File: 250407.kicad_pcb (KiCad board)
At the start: 2 copper layers, 390 x 180.2 mm, 227 parts, among them CN1 KEYBOARD_20PIN_MALE, CN10 LED_CONNECTOR, CN2 USER_PORT_CON, CN3 CASSETTE_PORT_CON, CN4 SERIAL_BUS_CON, CN5 AV_CONN, CN6 EXPANSION_PORT, CN7 POWER_CON, CN8 CONTROL_PORT, CN9 CONTROL_PORT, M1 MODULATOR_LONGBOARD, Q1 2SC1815, Q2 2SC1815, Q3 TP29B/2SD880, Q7 2SC1815, Q8 2SC1815, SW1 POWER_SWITCH, U1 CIA_U1, U10 4164-2, U11 4164-2, U12 4164-2, U13 74LS257, U14 74LS258, U15 74LS139, U16 4066_U28, U17 PLA_U17, U18 6581, U19 VIC, U2 CIA_U2, U20 556, U21 4164-2, U22 4164-2, U23 4164-2, U24 4164-2, U25 74LS257, U26 74LS373, U27 7408_U27, U28 4066_U28, U29 74LS74, U3 2364A, U30 74LS193, U31 74LS629N, U32 MC4044, U4 2364A, U5 2332A, U6 2114, U7 6510_MPU, U8 7406N, U9 4164-2, Y1 Crystal

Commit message: rename schematics and pcb libraries add C64-discrete-library for the missing symbols fix symbol references in sch and pcb
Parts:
- C1, C10, C100, C101, C103, C105, C11, C16, C18, C2, C200, C204, C205, C22, C25, C26, C27, C28, C29, C3, C30, C31, C32, C33, C37, C39, C4, C40, C41, C42, C43, C44, C45, C46, C47, C48, C49, C5, C50, C51, C52, C53, C54, C56, C59, C6, C60, C66, C67, C68, C7, C74, C82, C84, C85, C89, C9, C92, C93, C95, C96, C97, C98, C99: footprint KU-14194HB-RevB-KiCad:CAP_P5.08mm -> C64-pcb-library:CAP_P5.08mm
- C102, C107, C108, C12, C13, C14, C15, C17, C24, C34, C57, C62, C65, C8, C94: footprint KU-14194HB-RevB-KiCad:CAP_ELYT_RADIAL_P5.08mm_SMALL_RING -> C64-pcb-library:CAP_ELYT_RADIAL_P5.08mm_SMALL_RING
- C19, C88, C90: footprint KU-14194HB-RevB-KiCad:LARGE_ELECTROLYTIC_AXIAL_TH -> C64-pcb-library:LARGE_ELECTROLYTIC_AXIAL_TH
- C20, C21: footprint KU-14194HB-RevB-KiCad:CAP_POLY_100V_TH_P5.08_and_P12.07mm -> C64-pcb-library:CAP_POLY_100V_TH_P5.08_and_P12.07mm
- C203: footprint KU-14194HB-RevB-KiCad:CAPACITOR_RADIAL_P13.97_L9.9_D3.6 -> C64-pcb-library:CAPACITOR_RADIAL_P13.97_L9.9_D3.6
- C23, C38: footprint KU-14194HB-RevB-KiCad:CAP_AXIAL_P12.7mm -> C64-pcb-library:CAP_AXIAL_P12.7mm
- C36, C70, C83, C86, L2, R1, R100, R16, R17, R19, R2, R26, R28, R29, R3, R30, R31, R33, R34, R35, R36, R37, R38, R39, R4, R41, R42, R43, R44, R45, R5, R50, R51, R52, R53, R6, R7: footprint KU-14194HB-RevB-KiCad:RESISTOR -> C64-pcb-library:RESISTOR
- C91: footprint KU-14194HB-RevB-KiCad:CAP_ELYT_RADIAL_P5.08mm -> C64-pcb-library:CAP_ELYT_RADIAL_P5.08mm
- CN1: footprint KU-14194HB-RevB-KiCad:KEYBOARD_CON -> C64-pcb-library:KEYBOARD_CON
- CN10: footprint KU-14194HB-RevB-KiCad:LED_CON -> C64-pcb-library:LED_CON
- CN2: footprint KU-14194HB-RevB-KiCad:EDGE_CON_24P -> C64-pcb-library:EDGE_CON_24P
- CN3: footprint KU-14194HB-RevB-KiCad:EDGE_CON_12P_TAPE -> C64-pcb-library:EDGE_CON_12P_TAPE
- CN4: footprint KU-14194HB-RevB-KiCad:SERIAL_CON_DIN6 -> C64-pcb-library:SERIAL_CON_DIN6
- CN5: footprint KU-14194HB-RevB-KiCad:AV_CON_DIN8 -> C64-pcb-library:AV_CON_DIN8
- CN6: footprint KU-14194HB-RevB-KiCad:EXPANSION_PORT -> C64-pcb-library:EXPANSION_PORT
- CN7: footprint KU-14194HB-RevB-KiCad:POWER_CON_D7_250407 -> C64-pcb-library:POWER_CON_D7_250407
- CN8, CN9: footprint KU-14194HB-RevB-KiCad:JOYPORT_DB9 -> C64-pcb-library:JOYPORT_DB9
- CR1, CR2: footprint KU-14194HB-RevB-KiCad:ZENER_12.7mm -> C64-pcb-library:ZENER_12.7mm
- CR4: footprint KU-14194HB-RevB-KiCad:BRIDGE_RECTIFIER -> C64-pcb-library:BRIDGE_RECTIFIER
- CR5, CR6: footprint KU-14194HB-RevB-KiCad:RECTIFIER_TH_P12.7mm -> C64-pcb-library:RECTIFIER_TH_P12.7mm
- E1, E2: footprint KU-14194HB-RevB-KiCad:JUMPER_WIRE -> C64-pcb-library:JUMPER_WIRE
- F1: footprint KU-14194HB-RevB-KiCad:FUSE -> C64-pcb-library:FUSE
- FB1, FB10, FB11, FB12, FB13, FB14, FB15, FB16, FB17, FB18, FB19, FB2, FB20, FB21, FB22, FB23, FB3, FB4, FB5, FB7, FB8, FB9: footprint KU-14194HB-RevB-KiCad:FERRITE_BEAD_TH_P12.7mm -> C64-pcb-library:FERRITE_BEAD_TH_P12.7mm
- L4: footprint KU-14194HB-RevB-KiCad:CHOKE -> C64-pcb-library:CHOKE
- L5: footprint KU-14194HB-RevB-KiCad:INDUCTOR_P15.24mm -> C64-pcb-library:INDUCTOR_P15.24mm
- M1: footprint KU-14194HB-RevB-KiCad:MODULATOR_PORT_LONGBOARD -> C64-pcb-library:MODULATOR_PORT_LONGBOARD
- Q1, Q2, Q7, Q8: footprint KU-14194HB-RevB-KiCad:Q_NPN_ECB -> C64-pcb-library:Q_NPN_ECB
- Q3: footprint KU-14194HB-RevB-KiCad:TO-220-3_Horizontal_TabDown_250407 -> C64-pcb-library:TO-220-3_Horizontal_TabDown_250407
- R27: footprint KU-14194HB-RevB-KiCad:POTMETER -> C64-pcb-library:POTMETER
- RP1, RP2, RP3: footprint KU-14194HB-RevB-KiCad:RP_ARRAY_7WAY -> C64-pcb-library:RP_ARRAY_7WAY
- RP4: footprint KU-14194HB-RevB-KiCad:RP_ARRAY_9WAY -> C64-pcb-library:RP_ARRAY_9WAY
- SW1: footprint KU-14194HB-RevB-KiCad:POWER_SWITCH -> C64-pcb-library:POWER_SWITCH
- U1, U19, U2, U7: footprint KU-14194HB-RevB-KiCad:DIP40 -> C64-pcb-library:DIP40
- U10, U11, U12, U13, U14, U15, U21, U22, U23, U24, U25, U30, U31, U9: footprint KU-14194HB-RevB-KiCad:DIP16 -> C64-pcb-library:DIP16
- U16, U20, U27, U28, U29, U32, U8: footprint KU-14194HB-RevB-KiCad:DIP14 -> C64-pcb-library:DIP14
- U17, U18: footprint KU-14194HB-RevB-KiCad:DIP28 -> C64-pcb-library:DIP28
- U26: footprint KU-14194HB-RevB-KiCad:DIP20 -> C64-pcb-library:DIP20
- U3, U4, U5: footprint KU-14194HB-RevB-KiCad:DIP24 -> C64-pcb-library:DIP24
- U6: footprint KU-14194HB-RevB-KiCad:DIP18 -> C64-pcb-library:DIP18
- VR1, VR2: footprint KU-14194HB-RevB-KiCad:VREG_TO-220-3_Horizontal_TabDown -> C64-pcb-library:VREG_TO-220-3_Horizontal_TabDown
- Y1: footprint KU-14194HB-RevB-KiCad:CRYSTAL -> C64-pcb-library:CRYSTAL
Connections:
- C1 pad 1: /5V_FB3 -> Net-(C1-Pad1)
- C66 pad 1: CAN+5V -> Net-(C66-Pad1)
- C67 pad 1: /+Vc -> Net-(C67-Pad1)
- C82 pad 1: /+Vc -> Net-(C82-Pad1)
- CN7 pad 2: Earth -> Net-(CN7-Pad2)
- E1 pad 2: /jumper_select -> Net-(E1-Pad2)
- R27 pad 3: Net-(C108-Pad1) -> Net-(R27-Pad3)
- SW1 pad pe: (no net) -> Earth
- U27 pad 14: +5V -> Net-(U27-Pad14)
- U29 pad 1: Earth -> Net-(U29-Pad1)
- U29 pad 2: Earth -> Net-(U29-Pad2)
- U31 pad 1: Net-(C108-Pad1) -> Net-(R27-Pad3)

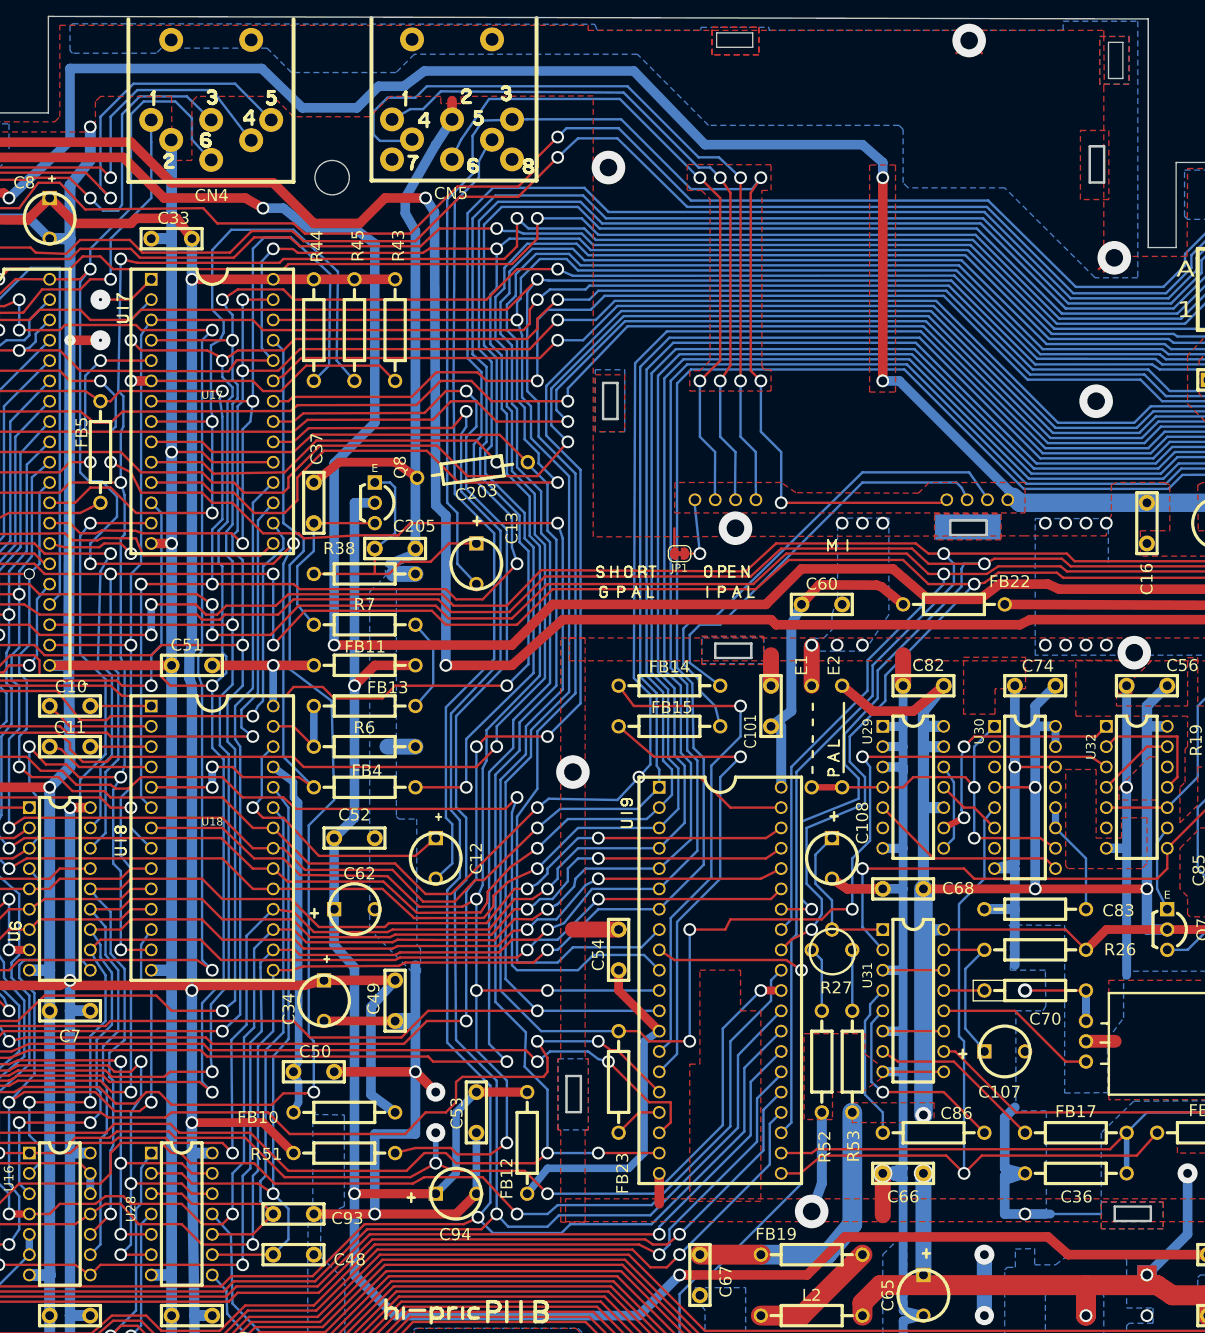
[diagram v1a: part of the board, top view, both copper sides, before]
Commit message: change Earth net to GND fix PCB DRC fix slanted PCB edge
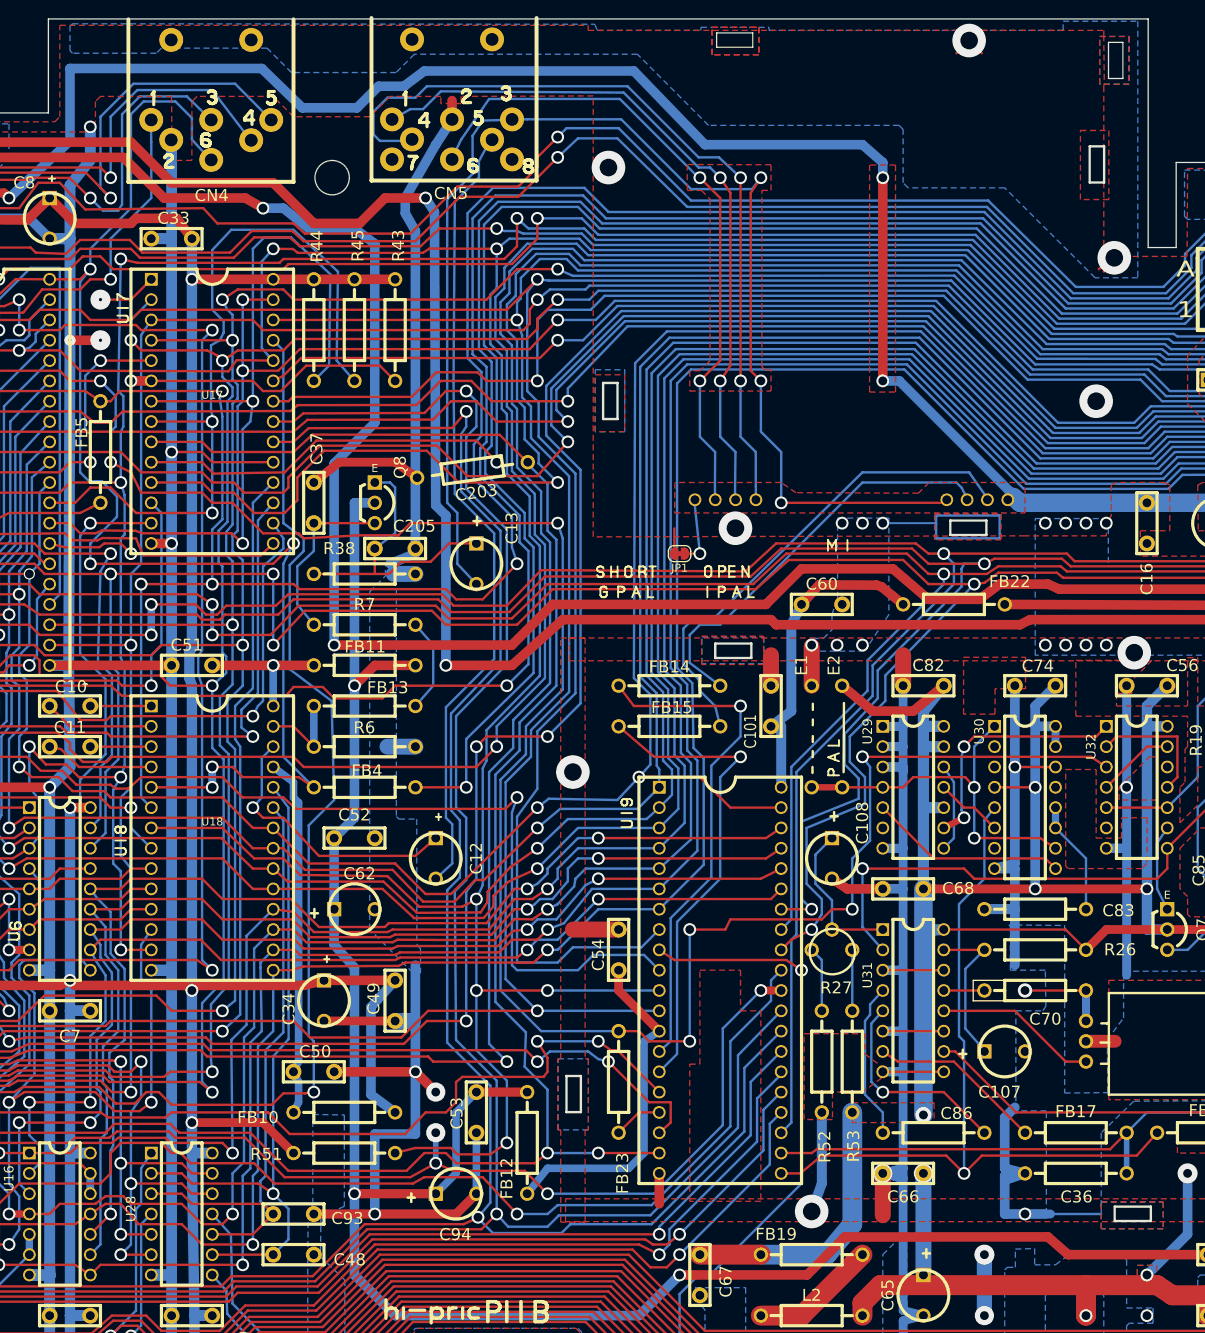
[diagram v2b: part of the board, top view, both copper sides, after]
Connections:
- C1 pad 1: Net-(C1-Pad1) -> /5V_FB3
- C1 pad 2: Earth -> GND
- C100 pad 1: Earth -> GND
- C101 pad 2: Earth -> GND
- C102 pad 2: Earth -> GND
- C103 pad 2: Earth -> GND
- C105 pad 1: Earth -> GND
- C107 pad 2: Earth -> GND
- C108 pad 2: Earth -> GND
- C14 pad 2: Earth -> GND
- C15 pad 2: Earth -> GND
- C16 pad 2: Earth -> GND
- C17 pad 2: Earth -> GND
- C19 pad 2: Earth -> GND
- C2 pad 2: Earth -> GND
- C200 pad 2: Earth -> GND
- C203 pad 1: Earth -> GND
- C204 pad 1: Earth -> GND
- C205 pad 2: Earth -> GND
- C22 pad 2: Earth -> GND
- C23 pad 2: Earth -> GND
- C24 pad 2: Earth -> GND
- C25 pad 2: Earth -> GND
- C26 pad 2: Earth -> GND
- C27 pad 2: Earth -> GND
- C28 pad 2: Earth -> GND
- C29 pad 1: Earth -> GND
- C3 pad 1: Earth -> GND
- C30 pad 2: Earth -> GND
- C31 pad 1: Earth -> GND
- C32 pad 1: Earth -> GND
- C33 pad 2: Earth -> GND
- C34 pad 2: Earth -> GND
- C36 pad 2: Earth -> GND
- C37 pad 2: Earth -> GND
- C39 pad 1: Earth -> GND
- C4 pad 1: Earth -> GND
- C40 pad 2: Earth -> GND
- C41 pad 2: Earth -> GND
- C42 pad 2: Earth -> GND
- C43 pad 2: Earth -> GND
- C44 pad 1: Earth -> GND
- C45 pad 2: Earth -> GND
- C46 pad 2: Earth -> GND
- C47 pad 2: Earth -> GND
- C48 pad 2: Earth -> GND
- C49 pad 2: Earth -> GND
- C5 pad 1: Earth -> GND
- C50 pad 2: Earth -> GND
- C51 pad 2: Earth -> GND
- C52 pad 2: Earth -> GND
- C53 pad 2: Earth -> GND
- C54 pad 2: Earth -> GND
- C56 pad 2: Earth -> GND
- C57 pad 2: Earth -> GND
- C59 pad 2: Earth -> GND
- C6 pad 1: Earth -> GND
- C60 pad 2: Earth -> GND
- C62 pad 2: Earth -> GND
- C65 pad 2: Earth -> GND
- C66 pad 1: Net-(C66-Pad1) -> CAN+5V
- C66 pad 2: Earth -> GND
- C67 pad 1: Net-(C67-Pad1) -> /+Vc
- C67 pad 2: Earth -> GND
- C68 pad 2: Earth -> GND
- C7 pad 2: Earth -> GND
- C74 pad 2: Earth -> GND
- C8 pad 2: Earth -> GND
- C82 pad 1: Net-(C82-Pad1) -> /+Vc
- C82 pad 2: Earth -> GND
- C83 pad 2: Earth -> GND
- C84 pad 2: Earth -> GND
- C88 pad 2: Earth -> GND
- C89 pad 2: Earth -> GND
- C9 pad 2: Earth -> GND
- C91 pad 2: Earth -> GND
- C92 pad 2: Earth -> GND
- C93 pad 2: Earth -> GND
- C94 pad 2: Earth -> GND
- C95 pad 2: Earth -> GND
- C96 pad 1: Earth -> GND
- C97 pad 1: Earth -> GND
- C98 pad 2: Earth -> GND
- C99 pad 1: Earth -> GND
- CN1 pad 1: Earth -> GND
- CN2 pad 1: Earth -> GND
- CN2 pad 12: Earth -> GND
- CN2 pad A: Earth -> GND
- CN2 pad N: Earth -> GND
- CN3 pad A,1: Earth -> GND
- CN4 pad 2: Earth -> GND
- CN5 pad 2: Earth -> GND
- CN6 pad 1: Earth -> GND
- CN6 pad 22: Earth -> GND
- CN6 pad A: Earth -> GND
- CN6 pad Z: Earth -> GND
- CN7 pad 1: Earth -> GND
- CN7 pad 3: Earth -> GND
- CN8 pad 8: Earth -> GND
- CN9 pad 8: Earth -> GND
- CR1 pad 2: Earth -> GND
- CR2 pad 2: Earth -> GND
- CR4 pad 3: Earth -> GND
- E1 pad 1: Earth -> GND
- E1 pad 2: Net-(E1-Pad2) -> /jumper_select
- FB20 pad 1: Earth -> GND
- JP1 pad 2: Earth -> GND
- Q2 pad 1: Earth -> GND
- R27 pad 3: Net-(R27-Pad3) -> Net-(C108-Pad1)
- R3 pad 2: Earth -> GND
- R38 pad 1: Earth -> GND
- R52 pad 2: Earth -> GND
- R6 pad 1: Earth -> GND
- SW1 pad pe: Earth -> GND
- U1 pad 1: Earth -> GND
- U10 pad 16: Earth -> GND
- U11 pad 16: Earth -> GND
- U12 pad 16: Earth -> GND
- U13 pad 8: Earth -> GND
- U14 pad 8: Earth -> GND
- U15 pad 8: Earth -> GND
- U16 pad 7: Earth -> GND
- U17 pad 14: Earth -> GND
- U17 pad 19: Earth -> GND
- U18 pad 14: Earth -> GND
- U19 pad 20: Earth -> GND
- U2 pad 1: Earth -> GND
- U20 pad 7: Earth -> GND
- U21 pad 16: Earth -> GND
- U22 pad 16: Earth -> GND
- U23 pad 16: Earth -> GND
- U24 pad 16: Earth -> GND
- U25 pad 8: Earth -> GND
- U26 pad 10: Earth -> GND
- U27 pad 14: Net-(U27-Pad14) -> +5V
- U27 pad 7: Earth -> GND
- U28 pad 7: Earth -> GND
- U29 pad 1: Net-(U29-Pad1) -> GND
- U29 pad 2: Net-(U29-Pad2) -> GND
- U29 pad 3: Earth -> GND
- U29 pad 7: Earth -> GND
- U3 pad 12: Earth -> GND
- U30 pad 14: Earth -> GND
- U30 pad 8: Earth -> GND
- U31 pad 1: Net-(R27-Pad3) -> Net-(C108-Pad1)
- U31 pad 11: Earth -> GND
- U31 pad 14: Earth -> GND
- U31 pad 3: Earth -> GND
- U31 pad 6: Earth -> GND
- U31 pad 8: Earth -> GND
- U31 pad 9: Earth -> GND
- U32 pad 7: Earth -> GND
- U4 pad 12: Earth -> GND
- U5 pad 12: Earth -> GND
- U6 pad 9: Earth -> GND
- U7 pad 21: Earth -> GND
- U8 pad 7: Earth -> GND
- U9 pad 16: Earth -> GND
- VR1 pad 3: Earth -> GND
- VR2 pad 3: Earth -> GND
- Y1 pad 3: Earth -> GND
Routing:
- net GND: track 0.00 -> 2456.0 mm, vias 0 -> 83
- net Earth: track 2427.7 -> 0.00 mm, vias 83 -> 0
- net (no net): track 111.3 -> 88.6 mm
- added copper zone on B.Cu, net CAN+5V
- added copper zone on F.Cu, net CAN+5V
- added copper zone on B.Cu, net GND
- added copper zone on F.Cu, net GND
- removed copper zone on B.Cu, net Earth
- removed copper zone on F.Cu, net Earth
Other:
- board size 390 x 180.2 mm -> 390 x 179.8 mm
- rule pad_to_mask_clearance: 0.051 -> 0

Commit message: update BRIDGE RECTIFIER symbol remove redundant tracks
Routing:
- net GND: track 2456.0 -> 2396.8 mm
- net +5V: track 2232.9 -> 2212.9 mm
- net Net-(C97-Pad2): track 22.0 -> 19.4 mm, vias 1 -> 0
